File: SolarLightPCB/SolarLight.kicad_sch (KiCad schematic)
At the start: 14 parts, among them J1 I2C, J2 Conn_01x06_Male, SW1 SW_Push, SW2 ON_OFF, U1 TP4056, U2 WeMos_D1_mini, U3 MCP1700-3302E

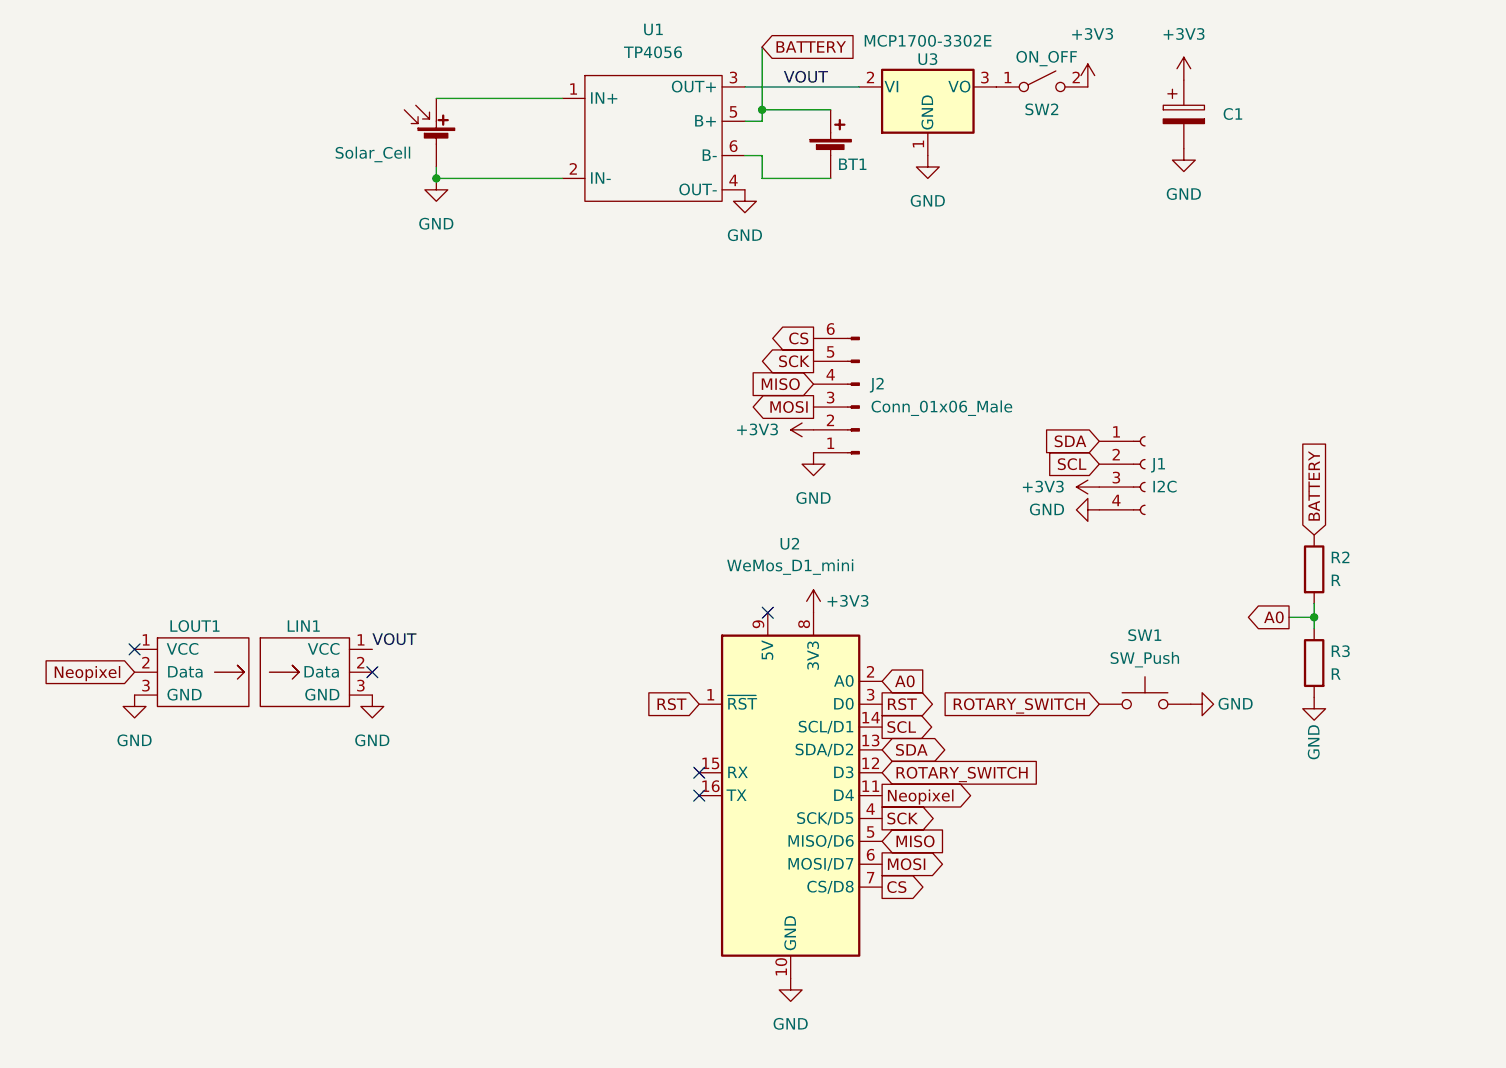
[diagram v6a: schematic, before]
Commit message: Remove the voltage regulator
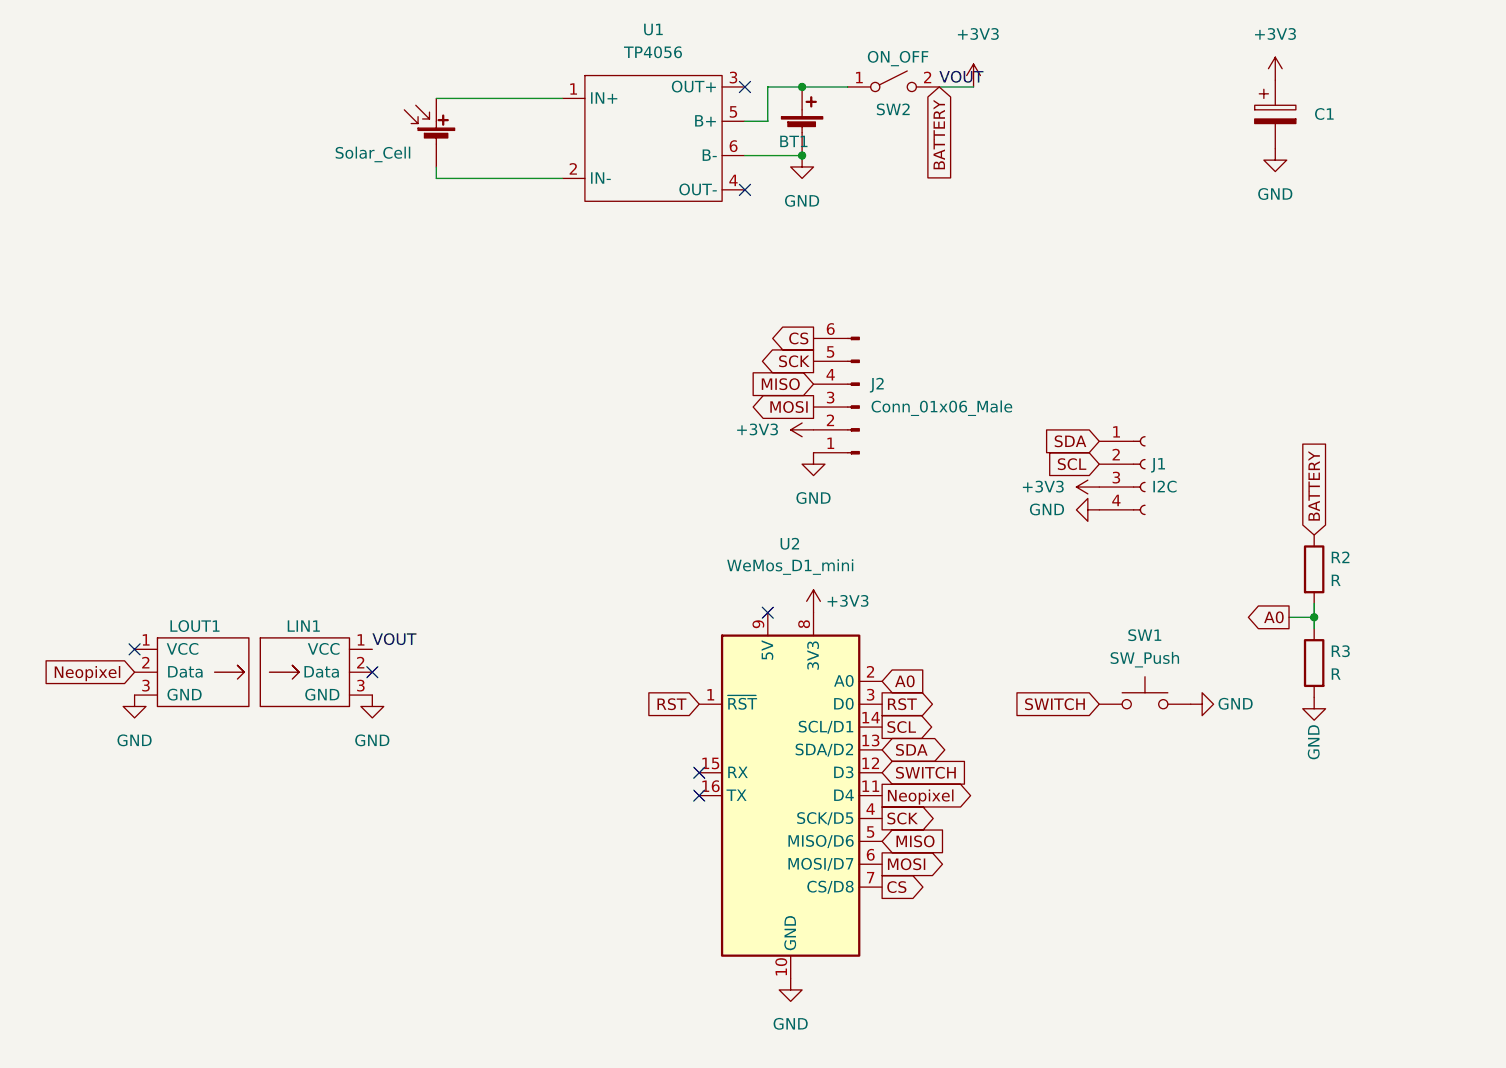
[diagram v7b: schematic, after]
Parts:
- removed U3: MCP1700-3302E, Package_TO_SOT_THT:TO-92L_Wide, symbol Regulator_Linear:L78L33_TO92
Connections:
- net +3V3: now also LIN1.1 (VCC), R2.1
- net GND: now also BT1.2 (-), U1.6 (B-); no longer SC1.2 (-), U1.2 (IN-), U1.4 (OUT-)
- net at SW2.1 (A): now also BT1.1 (+), U1.5 (B+)
- removed net BATTERY: BT1.1 (+), R2.1, U1.5 (B+)
- net ROTARY_SWITCH renamed SWITCH
- net VOUT: no longer names the net of U1.3 (OUT+)
- net VOUT: no longer LIN1.1 (VCC)
- new net: SC1.2 (-), U1.2 (IN-)
- no-connect marks 5 -> 7
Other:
- moved on the sheet: BT1, C1, SW2

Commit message: Add the missing capacitor to the schema
Fixing the warning because the pad of the charger module was removed
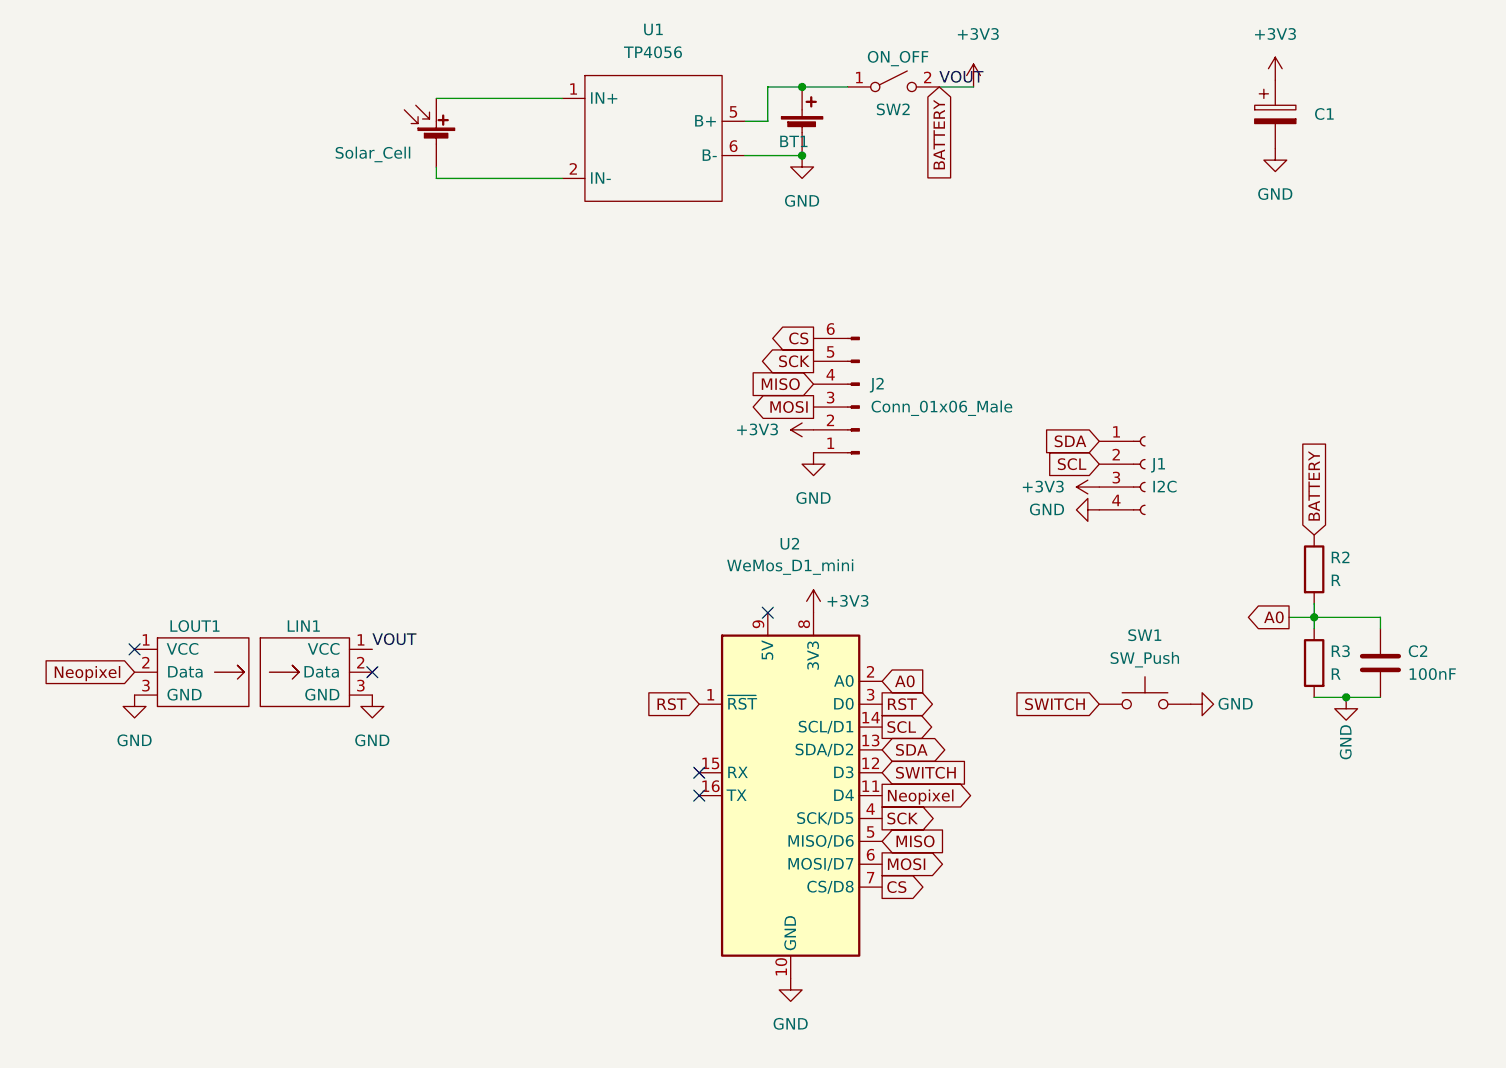
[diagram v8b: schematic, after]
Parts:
- added C2: 100nF, Capacitor_THT:C_Disc_D5.0mm_W2.5mm_P5.00mm, symbol Device:C
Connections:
- net GND: now also C2.2
- no-connect marks 7 -> 5
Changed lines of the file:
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@@
   (junction (at 157.48 38.1) (diameter 0) (color 0 0 0 0)
+  )
+  (junction (at 217.932 105.918) (diameter 0) (color 0 0 0 0)
   )
   (junction (at 214.376 97.028) (diameter 0) (color 0 0 0 0)
@@
   (no_connect (at 146.05 114.3))
   (no_connect (at 146.05 116.84))
-  (no_connect (at 151.13 38.1))
-  (no_connect (at 151.13 49.53))
+  (wire (pts (xy 214.63 97.028) (xy 221.742 97.028))
+    (stroke (width 0) (type default) (color 0 0 0 0))
+  )
   (wire (pts (xy 116.84 48.26) (xy 116.84 46.99))
     (stroke (width 0) (type default) (color 0 0 0 0))
@@
     (stroke (width 0) (type default) (color 0 0 0 0))
   )
+  (wire (pts (xy 214.376 105.918) (xy 217.932 105.918))
+    (stroke (width 0) (type default) (color 0 0 0 0))
+  )
   (wire (pts (xy 153.67 38.1) (xy 153.67 41.91))
     (stroke (width 0) (type default) (color 0 0 0 0))
@@
     (stroke (width 0) (type default) (color 0 0 0 0))
   )
+  (wire (pts (xy 217.932 105.918) (xy 221.742 105.918))
+    (stroke (width 0) (type default) (color 0 0 0 0))
+  )
   (wire (pts (xy 151.13 45.72) (xy 157.48 45.72))
     (stroke (width 0) (type default) (color 0 0 0 0))
   )
   (wire (pts (xy 157.48 38.1) (xy 153.67 38.1))
+    (stroke (width 0) (type default) (color 0 0 0 0))
+  )
+  (wire (pts (xy 221.742 97.028) (xy 221.742 98.298))
     (stroke (width 0) (type default) (color 0 0 0 0))
   )
@@
     (pin "2")
   )
-  (symbol (lib_id "power:GND") (at 214.376 105.918 0) (unit 1)
-    (in_bom yes) (on_board yes)
-    (property "Reference" "#PWR0115" (id 0) (at 214.376 112.268 0)
-      (effects (font (size 1.27 1.27)) hide)
-    )
-    (property "Value" "GND" (id 1) (at 214.376 112.903 90)
-      (effects (font (size 1.27 1.27)) (justify left))
-    )
-    (property "Footprint" "" (id 2) (at 214.376 105.918 0)
-      (effects (font (size 1.27 1.27)) hide)
-    )
-    (property "Datasheet" "" (id 3) (at 214.376 105.918 0)
+  (symbol (lib_id "power:GND") (at 217.932 105.918 0) (unit 1)
+    (in_bom yes) (on_board yes)
+    (property "Reference" "#PWR0115" (id 0) (at 217.932 112.268 0)
+      (effects (font (size 1.27 1.27)) hide)
+    )
+    (property "Value" "GND" (id 1) (at 217.932 112.903 90)
+      (effects (font (size 1.27 1.27)) (justify left))
+    )
+    (property "Footprint" "" (id 2) (at 217.932 105.918 0)
+      (effects (font (size 1.27 1.27)) hide)
+    )
+    (property "Datasheet" "" (id 3) (at 217.932 105.918 0)
       (effects (font (size 1.27 1.27)) hide)
     )
@@
     (pin "1")
     (pin "2")
-    (pin "3")
-    (pin "4")
     (pin "5")
     (pin "6")
@@
     )
     (pin "1")
+  )
+  (symbol (lib_id "Device:C") (at 221.742 102.108 0) (unit 1)
+    (in_bom yes) (on_board yes) (fields_autoplaced)
+    (property "Reference" "C2" (id 0) (at 224.79 100.8379 0)
+      (effects (font (size 1.27 1.27)) (justify left))
+    )
+    (property "Value" "100nF" (id 1) (at 224.79 103.3779 0)
+      (effects (font (size 1.27 1.27)) (justify left))
+    )
+    (property "Footprint" "Capacitor_THT:C_Disc_D5.0mm_W2.5mm_P5.00mm" (id 2) (at 222.7072 105.918 0)
+      (effects (font (size 1.27 1.27)) hide)
+    )
+    (property "Datasheet" "~" (id 3) (at 221.742 102.108 0)
+      (effects (font (size 1.27 1.27)) hide)
+    )
+    (pin "1")
+    (pin "2")
   )
   (symbol (lib_id "Switch:SW_SPST") (at 167.64 38.1 0) (unit 1)
@@
       (reference "C1") (unit 1) (value "C_Polarized") (footprint "Capacitor_THT:CP_Radial_D5.0mm_P2.50mm")
     )
+    (path "/9c2f0fd6-e41a-416c-b2be-65aa3517df2d"
+      (reference "C2") (unit 1) (value "100nF") (footprint "Capacitor_THT:C_Disc_D5.0mm_W2.5mm_P5.00mm")
+    )
     (path "/b014f64b-63d7-4679-a15c-8f4cf024b19d"
